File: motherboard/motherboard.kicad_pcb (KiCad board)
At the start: 2 copper layers, 47.6 x 70.5 mm, 27 parts, among them J1 Conn_01x12, J2 Conn_01x12, J3 Conn_01x12, J4 Conn_01x12, J5 Conn_01x12, J6 Conn_01x12, J7 USB_C_Receptacle_USB2.0, SW1 SW_Push, SW2 SW_Push, U1 SRV05-4, U2 M3406-ADJ, U3 ESP32-S3-WROOM-1

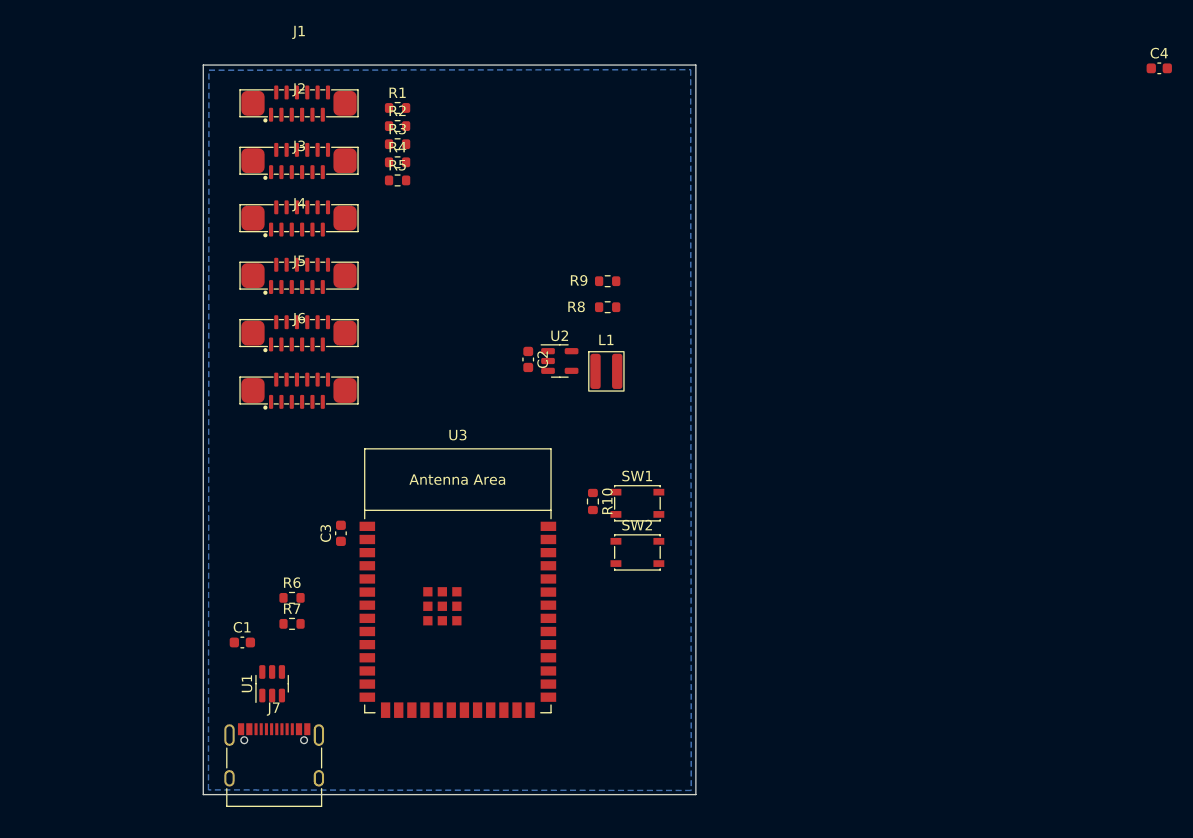
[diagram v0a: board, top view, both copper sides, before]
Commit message: motherboard basics routed
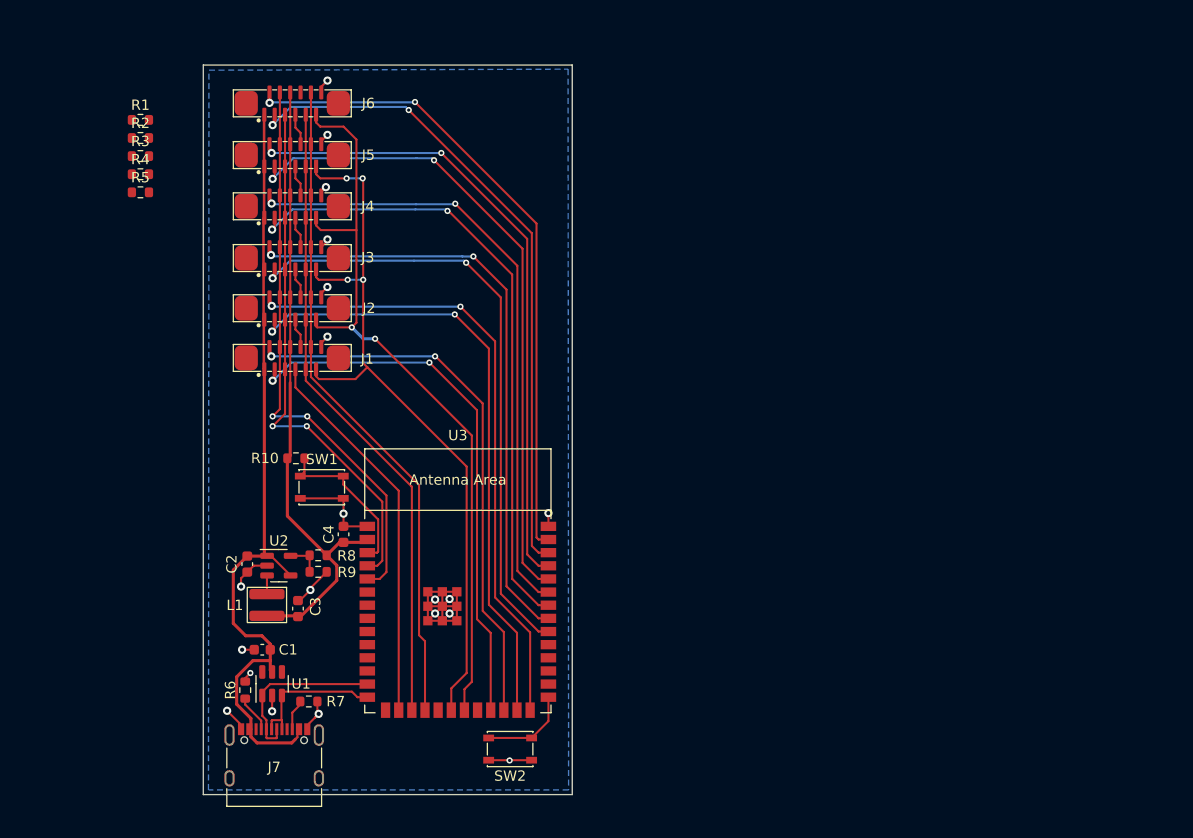
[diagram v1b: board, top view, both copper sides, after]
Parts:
- moved C4 90.8 mm to (58.1, 91.2), turned to 90 degrees
- moved L1 39.8 mm to (50.8, 98.1), turned to -90 degrees
- moved R9 39.6 mm to (55.7, 94.9), turned to 180 degrees
- moved R8 36.8 mm to (55.7, 93.3)
- moved C2 33.6 mm to (48.9, 94.1)
- moved U2 33.6 mm to (51.9, 94.3)
- moved SW1 30.5 mm to (56.0, 86.7), turned to 180 degrees
- moved R10 29.0 mm to (53.5, 83.9), turned to 0 degrees
- moved J6 27.8 mm to (53.2, 49.6)
- moved R1 24.9 mm to (38.5, 51.2)
- moved R2 24.9 mm to (38.5, 53.0)
- moved R3 24.9 mm to (38.5, 54.7)
- moved R4 24.9 mm to (38.5, 56.5)
- moved R5 24.9 mm to (38.5, 58.2)
- moved J1 24.6 mm to (53.2, 74.2)
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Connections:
- C1 pad 2: /Vusb -> /VIN
- J4 pad 1: unconnected-(J4-Pin_1-Pad1) -> /VIN
- J4 pad 2: unconnected-(J4-Pin_2-Pad2) -> /SDA4
- J4 pad 3: unconnected-(J4-Pin_3-Pad3) -> /SCL4
- U1 pad 3: unconnected-(U1-IO2-Pad3) -> /D+
- U1 pad 4: /D+ -> unconnected-(U1-IO3-Pad4)
- U1 pad 5: /Vusb -> /VIN
- U3 pad 11: /SS -> /microcontroller/GPIO18
- U3 pad 12: /SCL1 -> /microcontroller/GPIO8
- U3 pad 15: /SCL6 -> /microcontroller/GPIO3
- U3 pad 16: /microcontroller/GPIO46 -> /MOSI1
- U3 pad 17: /microcontroller/GPIO9 -> /SCLK
- U3 pad 18: /microcontroller/GPIO10 -> /SS
- U3 pad 20: /microcontroller/GPIO12 -> /POL1
- U3 pad 21: /microcontroller/GPIO13 -> /POL2
- U3 pad 23: /microcontroller/GPIO21 -> /SCL1
- U3 pad 25: /POL1 -> /SCL2
- U3 pad 26: /POL2 -> /SDA2
- U3 pad 32: /SDA4 -> /SCL3
- U3 pad 33: /SCL5 -> /SDA3
- U3 pad 34: /SCL3 -> /SCL4
- U3 pad 35: /SDA3 -> /SDA4
- U3 pad 36: unconnected-(U3-U0RXD/GPIO44/CLK_OUT2-Pad36) -> /SCL5
- U3 pad 37: unconnected-(U3-U0TXD/GPIO43/CLK_OUT1-Pad37) -> /SDA5
- U3 pad 38: /SCLK -> /SCL6
- U3 pad 39: /MISO1 -> /SDA6
- U3 pad 4: /SDA6 -> /IN-
- U3 pad 5: /MISO6 -> /IN+
- U3 pad 6: /SCL2 -> /microcontroller/GPIO6
- U3 pad 7: /SDA2 -> /microcontroller/GPIO7
- U3 pad 8: /SCL4 -> /microcontroller/GPIO15
- U3 pad 9: /SDA5 -> /microcontroller/GPIO16
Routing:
- net /VIN: track 0.00 -> 78.2 mm
- net /POL2: track 0.00 -> 75.4 mm, vias 0 -> 2
- net /POL1: track 0.00 -> 73.2 mm, vias 0 -> 4
- net /SS: track 0.00 -> 64.3 mm
- net /SCL6: track 0.00 -> 64.0 mm, vias 0 -> 2
- net /SCL5: track 0.00 -> 63.4 mm, vias 0 -> 2
- net /SDA6: track 0.00 -> 63.2 mm, vias 0 -> 2
- net /SDA5: track 0.00 -> 62.1 mm, vias 0 -> 2
- net /VDD: track 0.00 -> 62.0 mm
- net /SCL4: track 0.00 -> 61.8 mm, vias 0 -> 2
- net /SCLK: track 0.00 -> 61.8 mm
- net /SDA2: track 0.00 -> 61.0 mm, vias 0 -> 2
- net /SDA4: track 0.00 -> 60.5 mm, vias 0 -> 2
- net /SCL2: track 0.00 -> 60.3 mm, vias 0 -> 2
- net /SCL3: track 0.00 -> 59.9 mm, vias 0 -> 2
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- added copper zone on B.Cu, net GND
- removed copper zone on B.Cu, net (none)
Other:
- board size 47.6 x 70.5 mm -> 35.6 x 70.5 mm

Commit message: reroute motherboard: no traces under antenna
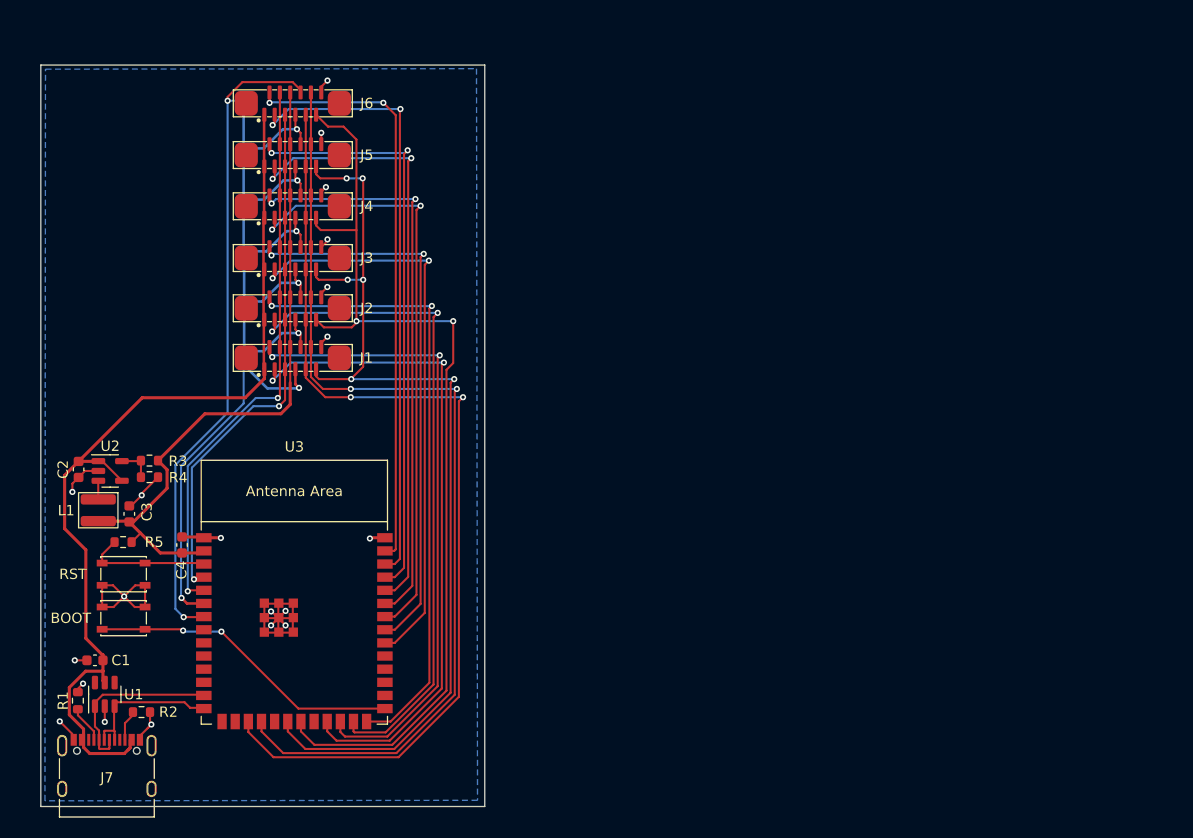
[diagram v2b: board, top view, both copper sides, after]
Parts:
- removed the R1 at (38.5, 51.2)
- removed the R2 at (38.5, 53.0)
- removed the R3 at (38.5, 54.7)
- removed the R4 at (38.5, 56.5)
- removed the R5 at (38.5, 58.2)
- added JP1: SolderJumper_2_Open, Jumper:SolderJumper-2_P1.3mm_Open_RoundedPad1.0x1.5mm, B.Cu at (48.5, 74.2)
- added JP2: SolderJumper_2_Bridged, Jumper:SolderJumper-2_P1.3mm_Bridged_RoundedPad1.0x1.5mm, B.Cu at (48.5, 69.4)
- added JP3: SolderJumper_2_Bridged, Jumper:SolderJumper-2_P1.3mm_Bridged_RoundedPad1.0x1.5mm, B.Cu at (48.5, 64.5)
- added JP4: SolderJumper_2_Bridged, Jumper:SolderJumper-2_P1.3mm_Bridged_RoundedPad1.0x1.5mm, B.Cu at (48.5, 59.5)
- added JP5: SolderJumper_2_Bridged, Jumper:SolderJumper-2_P1.3mm_Bridged_RoundedPad1.0x1.5mm, B.Cu at (48.5, 54.6)
- added JP6: SolderJumper_2_Bridged, Jumper:SolderJumper-2_P1.3mm_Bridged_RoundedPad1.0x1.5mm, B.Cu at (48.5, 49.6)
- J1, J2, J3, J4, J5, J6: value Conn_01x12 -> Conn_01x12_MountingPin; footprint Library:Jushuo_AFC11-S12I -> Optacon_common:Jushuo_AFC11-S12I
- L1: value 4.7µH -> 3.3µH
- SW1: value SW_Push -> RST
- SW2: value SW_Push -> BOOT
- moved SW2 39.4 mm to (36.9, 99.3), turned to 0 degrees
- moved SW1 20.9 mm to (36.9, 95.1)
- moved C2 18.7 mm to (32.5, 85.0)
- moved R3 18.7 mm to (39.4, 84.1)
- moved R4 18.7 mm to (39.4, 85.7)
- moved L1 18.7 mm to (34.5, 88.9)
- moved U2 18.7 mm to (35.6, 85.1)
- moved C3 18.7 mm to (37.5, 89.3)
- moved R5 18.6 mm to (36.9, 92.0), turned to 180 degrees
- moved J7 16.2 mm to (35.3, 114.8)
- moved R1 16.2 mm to (32.5, 107.3)
- moved U1 16.2 mm to (35.1, 106.7)
- moved C1 16.2 mm to (34.1, 103.4)
- moved R2 16.2 mm to (38.6, 108.4)
- moved U3 15.8 mm to (53.4, 99.8)
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- renumbered R6 to R1, R7 to R2, R8 to R3, R9 to R4, R10 to R5
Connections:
- U3 pad 16: /MOSI1 -> /microcontroller/GPIO46
- U3 pad 6: /microcontroller/GPIO6 -> /MOSI1
- U3 pad 7: /microcontroller/GPIO7 -> /MISO6
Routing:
- net /MISO6: track 0.00 -> 64.6 mm, vias 0 -> 2
- net /SCLK: track 61.8 -> 95.3 mm, vias 0 -> 2
- net /SS: track 64.3 -> 94.5 mm, vias 0 -> 2
- net Net-(U3-GPIO0/BOOT): track 8.76 -> 30.5 mm, vias 0 -> 2
- net /POL1: track 73.2 -> 94.9 mm, vias 4 -> 6
- net /POL2: track 75.4 -> 94.9 mm
- net /VIN: track 78.2 -> 91.5 mm
- net /SCL1: track 53.1 -> 64.5 mm
- net /MISO2: track 2.91 -> 12.5 mm, vias 0 -> 1
- net /MISO5: track 3.06 -> 12.7 mm, vias 0 -> 1
- net /MISO4: track 3.01 -> 12.6 mm, vias 0 -> 1
- net /MISO3: track 3.06 -> 12.7 mm, vias 0 -> 1
- net /MISO1: track 2.86 -> 12.4 mm, vias 0 -> 1
- net /SDA1: track 53.8 -> 62.0 mm
- net /SDA6: track 63.2 -> 56.8 mm
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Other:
- board size 35.6 x 70.5 mm -> 42.9 x 71.7 mm

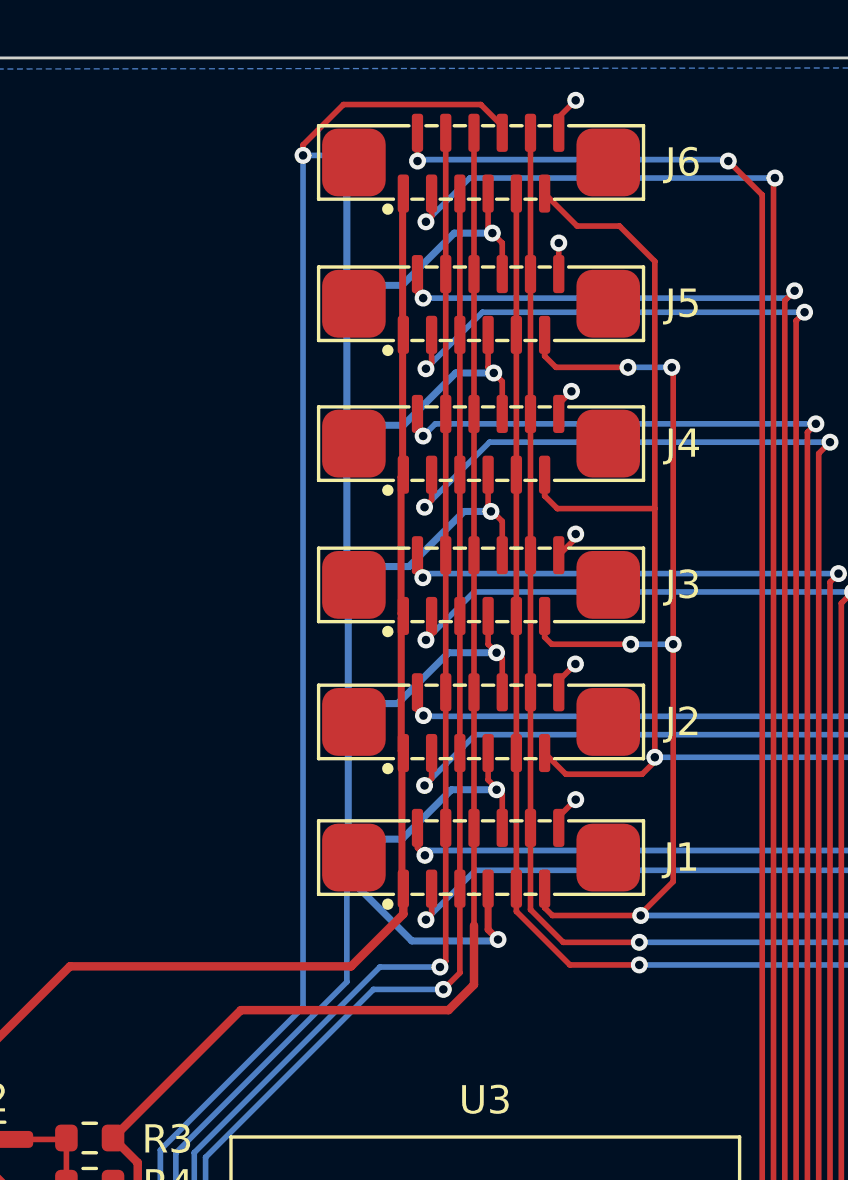
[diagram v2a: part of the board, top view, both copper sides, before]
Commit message: fpc connector mounting points
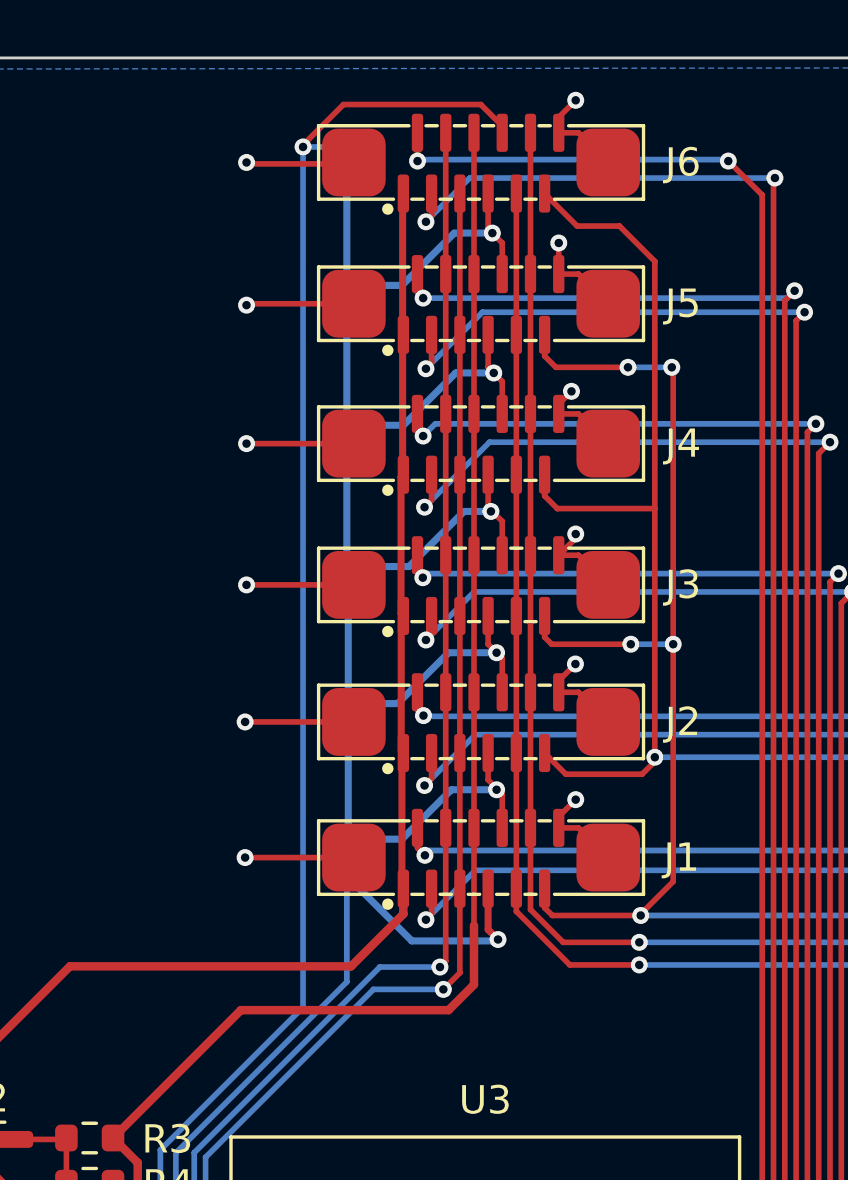
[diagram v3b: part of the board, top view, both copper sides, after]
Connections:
- J1 pad MP: unconnected-(J1-MountPin-PadMP) -> GND
- J2 pad MP: unconnected-(J2-MountPin-PadMP) -> GND
- J3 pad MP: unconnected-(J3-MountPin-PadMP) -> GND
- J4 pad MP: unconnected-(J4-MountPin-PadMP) -> GND
- J5 pad MP: unconnected-(J5-MountPin-PadMP) -> GND
- J6 pad MP: unconnected-(J6-MountPin-PadMP) -> GND
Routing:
- net GND: track 64.2 -> 100.3 mm, vias 20 -> 26

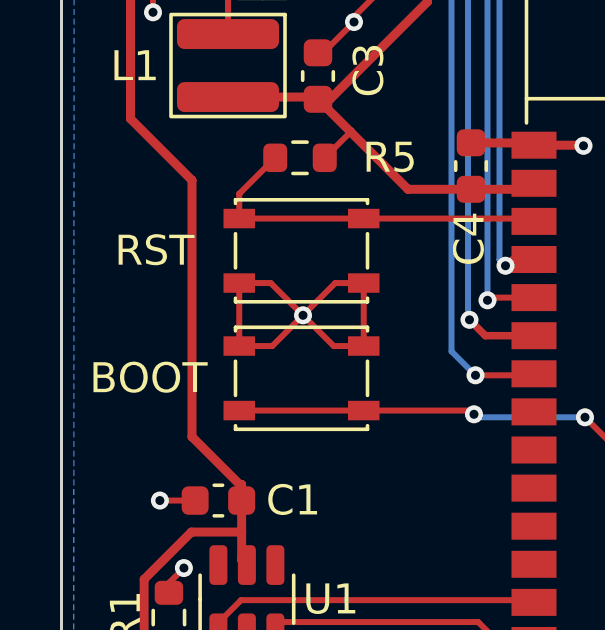
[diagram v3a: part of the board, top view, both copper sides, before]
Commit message: motherboard: buttons silkscreen
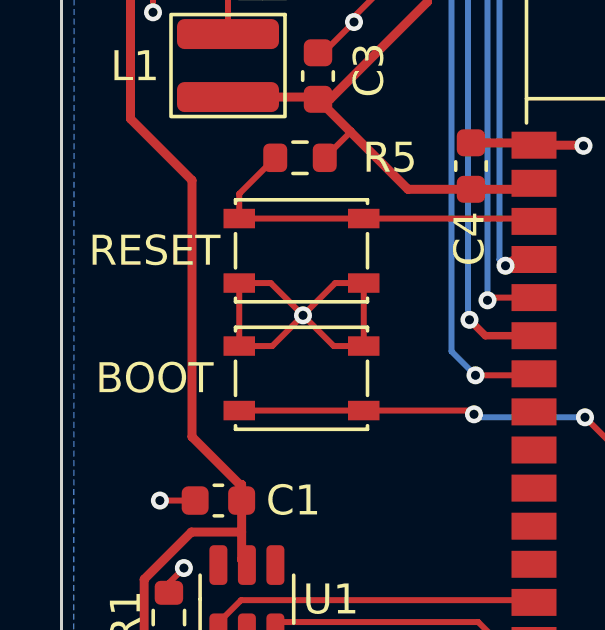
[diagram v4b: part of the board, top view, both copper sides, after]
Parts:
- SW1: value RST -> RESET
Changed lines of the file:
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@@
         (effects (font (size 1 1) (thickness 0.15)))
     )
-    (fp_text value "BOOT" (at -5.1 0) (layer "F.SilkS")
+    (fp_text value "BOOT" (at -4.9 0) (layer "F.SilkS")
         (effects (font (size 1 1) (thickness 0.15)))
     )
@@
         (effects (font (size 1 1) (thickness 0.15)))
     )
-    (fp_text value "RST" (at 4.9 0) (layer "F.SilkS")
-        (effects (font (size 1 1) (thickness 0.15)))
-    )
+    (fp_text value "RESET" (at 4.9 0) (layer "F.SilkS")
+        (effects (font (size 1 1) (thickness 0.15)))
+    )
